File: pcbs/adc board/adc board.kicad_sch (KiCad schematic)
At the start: 11 parts, among them IC1 ADS122C04IPWR, J1 Screw_Terminal_01x06, J5 Screw_Terminal_01x07

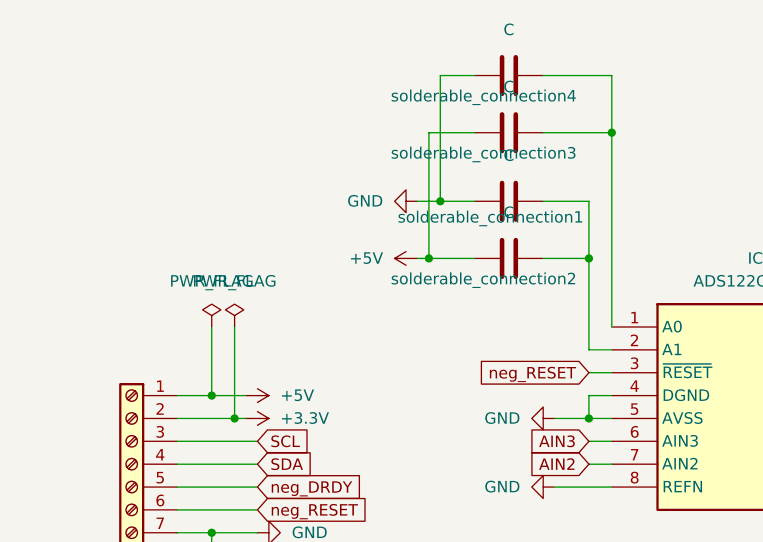
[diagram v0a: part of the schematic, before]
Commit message: 3.3 voltage level to address selection
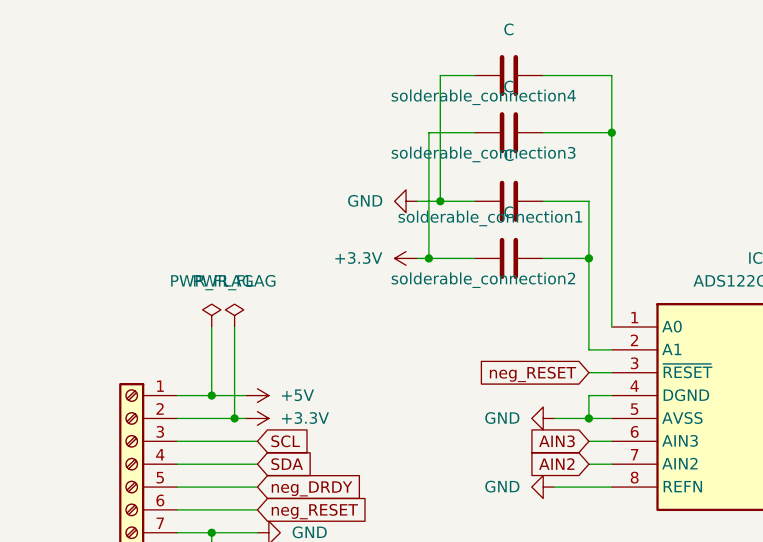
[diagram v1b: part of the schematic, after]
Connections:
- net +3.3V: now also solderable_connection2.1, solderable_connection3.1
- net +5V: no longer solderable_connection2.1, solderable_connection3.1
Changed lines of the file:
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@@
 (kicad_sch
-	(version 20231120)
+	(version 20250114)
 	(generator "eeschema")
-	(generator_version "8.0")
+	(generator_version "9.0")
 	(paper "A4")
 	(junction
@@
 		(on_board yes)
 		(dnp no)
-		(fields_autoplaced yes)
 		(property "Reference" "#PWR014"
 			(at 50.8 48.26 0)
@@
 			)
 		)
-		(property "Value" "+5V"
-			(at 43.18 48.2599 90)
-			(effects
-				(font
-					(size 1.27 1.27)
-				)
-				(justify left)
+		(property "Value" "+3.3V"
+			(at 40.386 48.26 90)
+			(effects
+				(font
+					(size 1.27 1.27)
+				)
 			)
 		)
@@
 		)
 	)
+	(embedded_fonts no)
 )

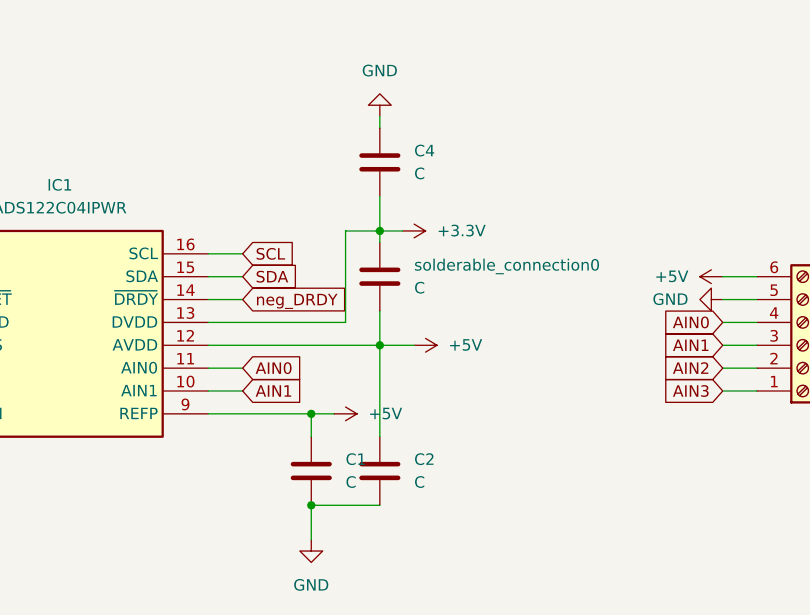
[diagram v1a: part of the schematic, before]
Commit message: labels added
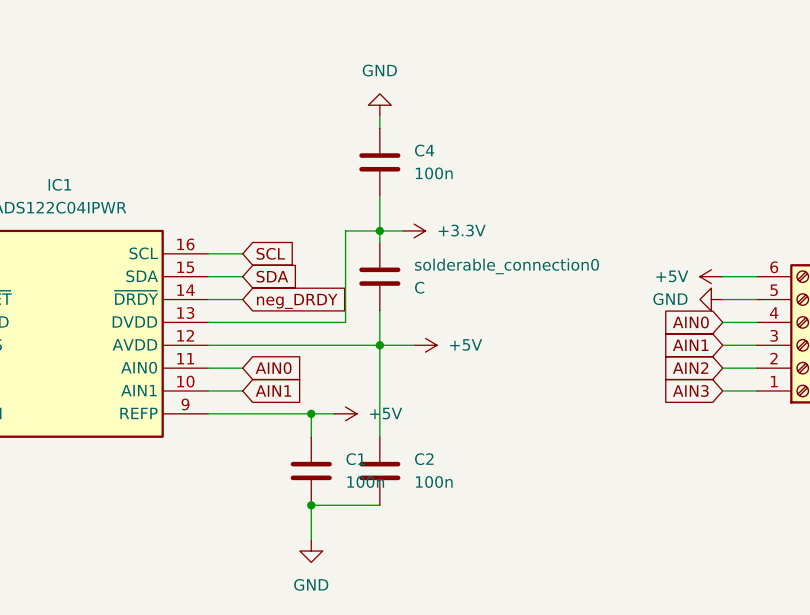
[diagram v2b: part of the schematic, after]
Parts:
- C1, C2, C4: value C -> 100n

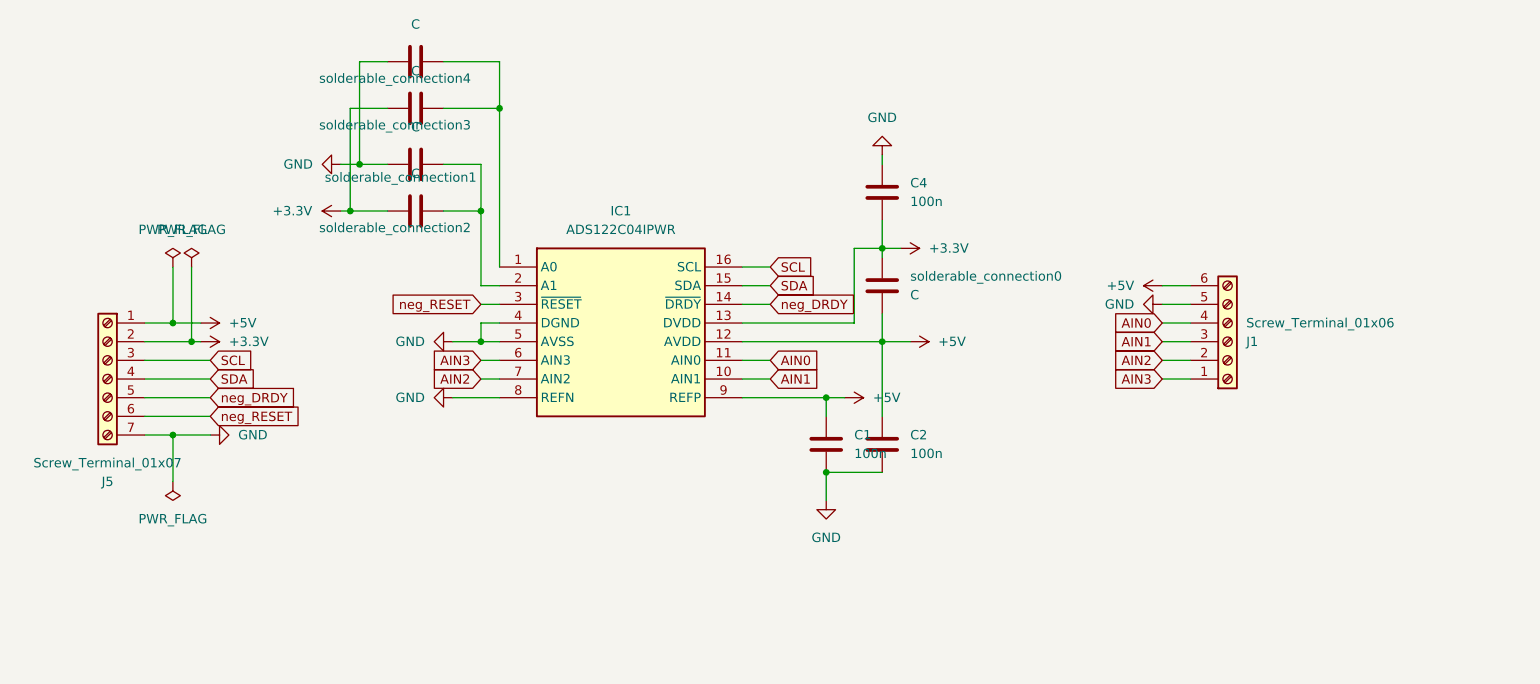
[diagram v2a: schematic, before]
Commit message: ADC kicad labels adjusted
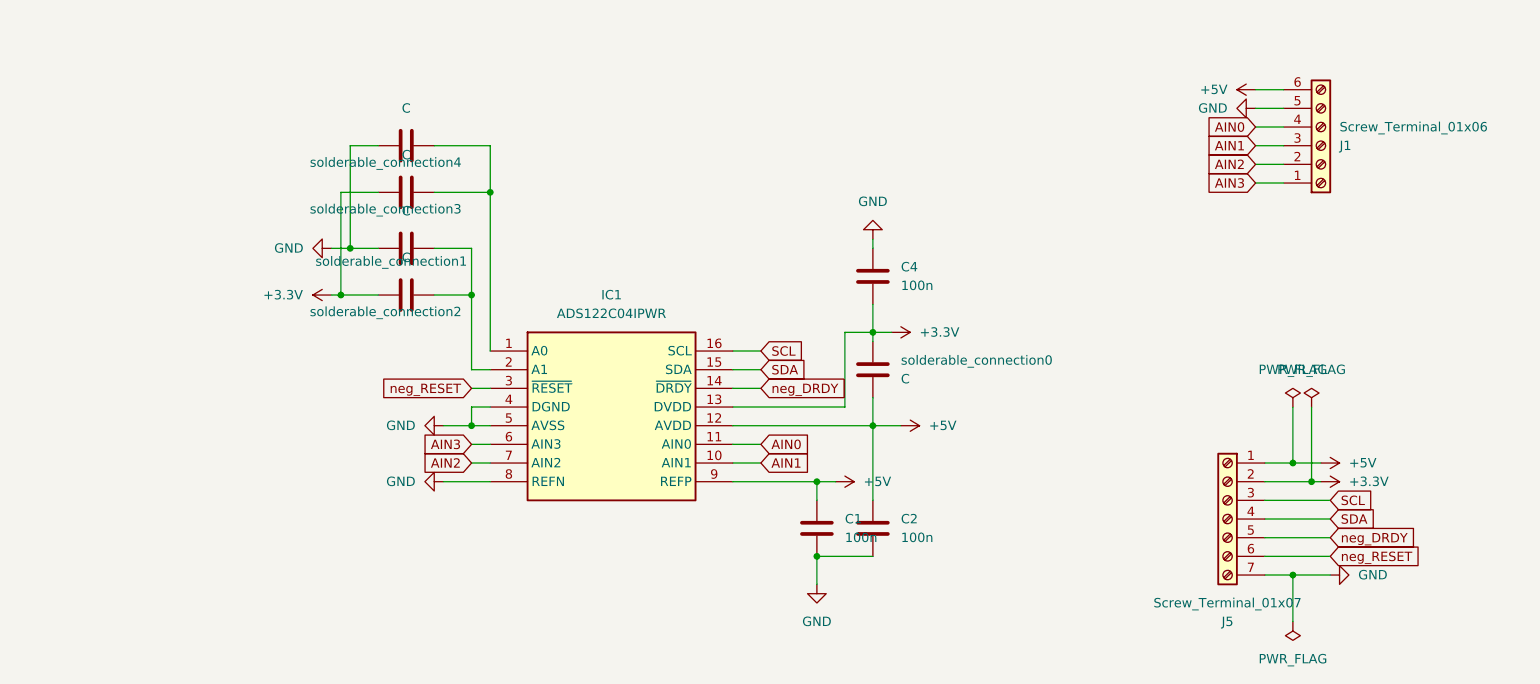
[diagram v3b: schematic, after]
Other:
- moved on the sheet: C1, C2, C4, IC1, J1, J5, solderable_connection0, solderable_connection1, solderable_connection2, solderable_connection3, solderable_connection4
